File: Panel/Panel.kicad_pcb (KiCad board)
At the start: 2 copper layers, 30.2 x 128.5 mm, 0 parts

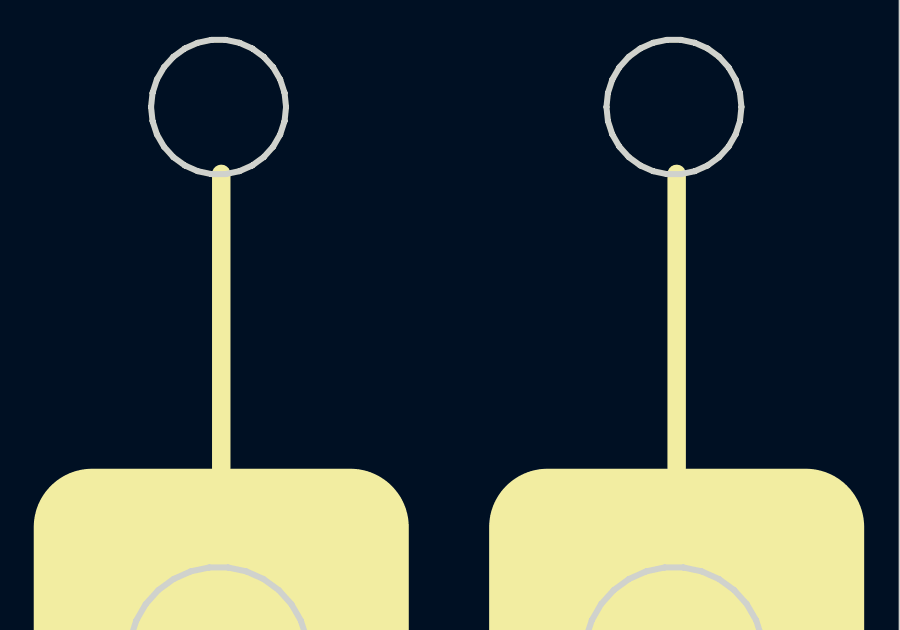
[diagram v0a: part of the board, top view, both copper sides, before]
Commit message: :sparkles: Add text "Make Clipping Gate Again" to panel
Idea by Patrick! :)
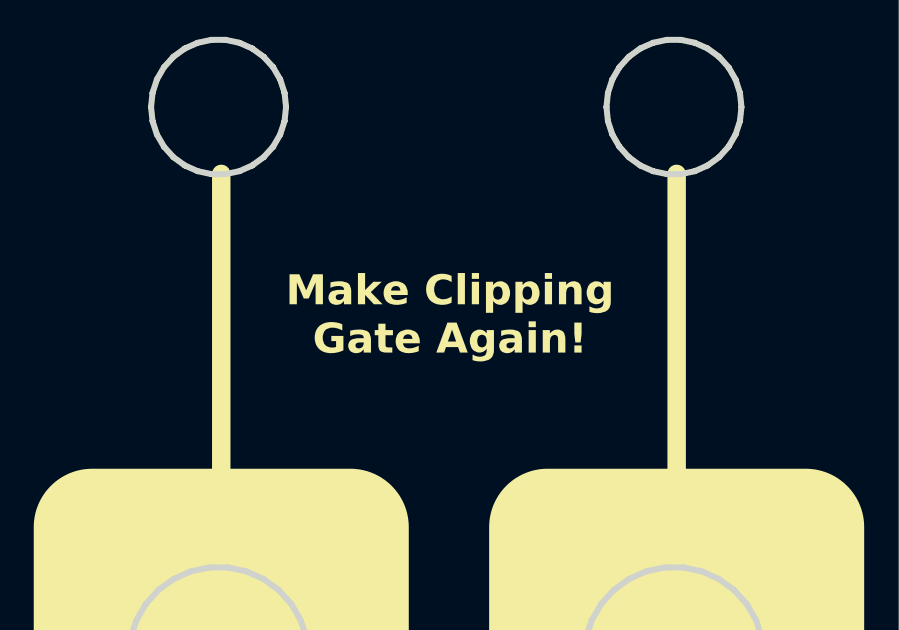
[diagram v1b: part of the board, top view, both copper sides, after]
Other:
- board text added: "Make Clipping Gate Again!"
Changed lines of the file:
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@@
     (effects (font (size 2.5 2.5) (thickness 0.3)) (justify bottom))
+  )
+  (gr_text "Make Clipping\nGate Again!" (at 120.0912 134.9756) (layer "F.SilkS")
+    (effects (font (size 1 1) (thickness 0.2) bold) (justify bottom))
   )
   (gr_text "CLIP\n" (at 112.5 155.15) (layer "F.SilkS")
